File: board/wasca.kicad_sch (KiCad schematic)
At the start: 64 parts, among them CN1 CARTRIDGE_EDGE_CONNECTOR, CN2 TFP09-2-12B, CN3 Conn_02x02_Odd_Even, CN4 SODIMM-200, CN5 693063020911, U1 74ALVC164245, U10 SN74LVC1T45DBV, U11 SN74LVC1T45DBV, U12 SN74LVC1T45DBV, U13 ESP32_CAM_HALF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

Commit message: "Endorsed  by SHIRO!" logo
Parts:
- added SHIRO!1: SHIRO_LOGO, wasca:SHIRO!, symbol wasca:KICAD_LOGO
- TP2: value (none) -> TestPoint; footprint (none) -> wasca:TEST_PAD
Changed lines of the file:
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@@
     (pin "B9")
+  )
+  (symbol (lib_id "wasca:KICAD_LOGO") (at 468.63 165.1 0) (unit 1)
+    (in_bom yes) (on_board yes)
+    (property "Reference" "SHIRO!1" (id 0) (at 476.9612 163.9316 0)
+      (effects (font (size 1.27 1.27)) (justify left))
+    )
+    (property "Value" "SHIRO_LOGO" (id 1) (at 476.9612 166.243 0)
+      (effects (font (size 1.27 1.27)) (justify left))
+    )
+    (property "Footprint" "wasca:SHIRO!" (id 2) (at 468.63 165.1 0))
+    (property "Datasheet" "" (id 3) (at 468.63 165.1 0)
+      (effects (font (size 1.27 1.27)) hide)
+    )
   )
   (symbol (lib_id "Device:R") (at 739.14 78.74 0) (mirror y) (unit 1)
@@
       (effects (font (size 1.27 1.27)) (justify left))
     )
-    (property "Value" "" (id 1) (at 716.28 192.2779 0)
-      (effects (font (size 1.27 1.27)) (justify left))
-    )
-    (property "Footprint" "" (id 2) (at 718.82 194.31 0)
+    (property "Value" "TestPoint" (id 1) (at 716.28 192.2779 0)
+      (effects (font (size 1.27 1.27)) (justify left))
+    )
+    (property "Footprint" "wasca:TEST_PAD" (id 2) (at 718.82 194.31 0)
       (effects (font (size 1.27 1.27)) hide)
     )
@@
       (reference "SEGATA1") (unit 1) (value "LOGO") (footprint "wasca:Segata_Sanshiro")
     )
+    (path "/4f18e9dd-59f1-4eb2-8a59-104ed488d908"
+      (reference "SHIRO!1") (unit 1) (value "SHIRO_LOGO") (footprint "wasca:SHIRO!")
+    )
     (path "/d276ace0-aa98-4013-94e5-a87cfcb3830a"

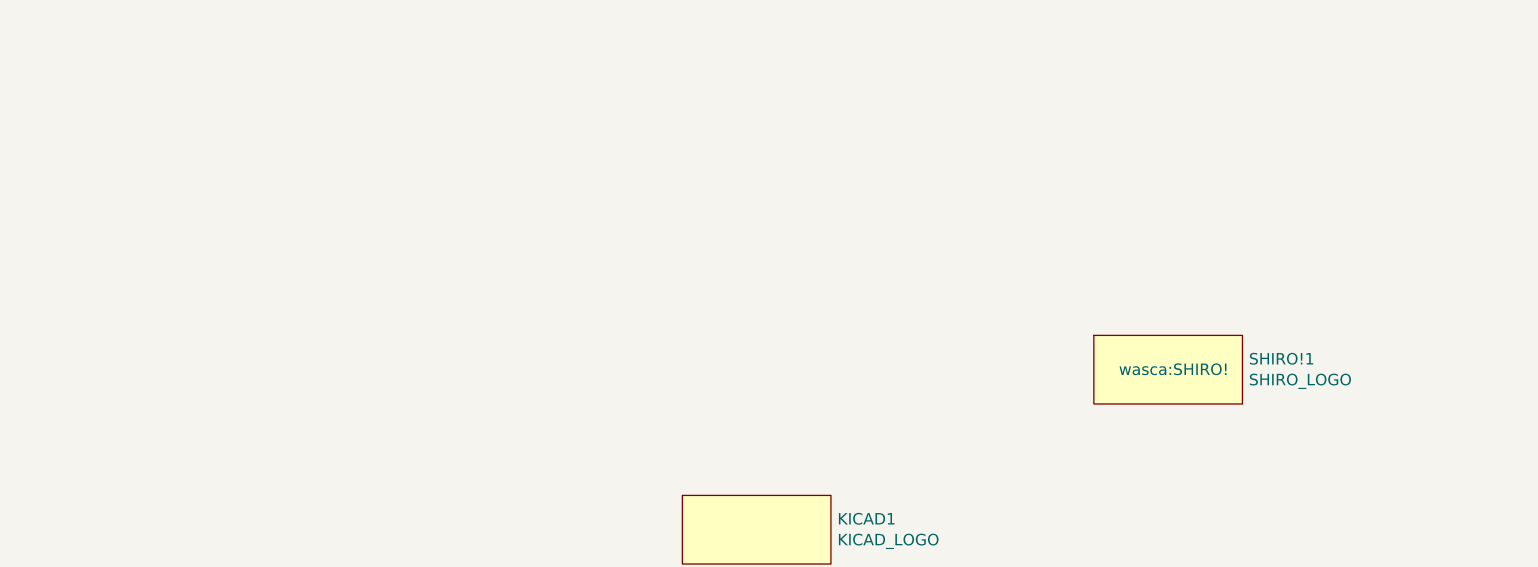
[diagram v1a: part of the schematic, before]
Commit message: Logo update
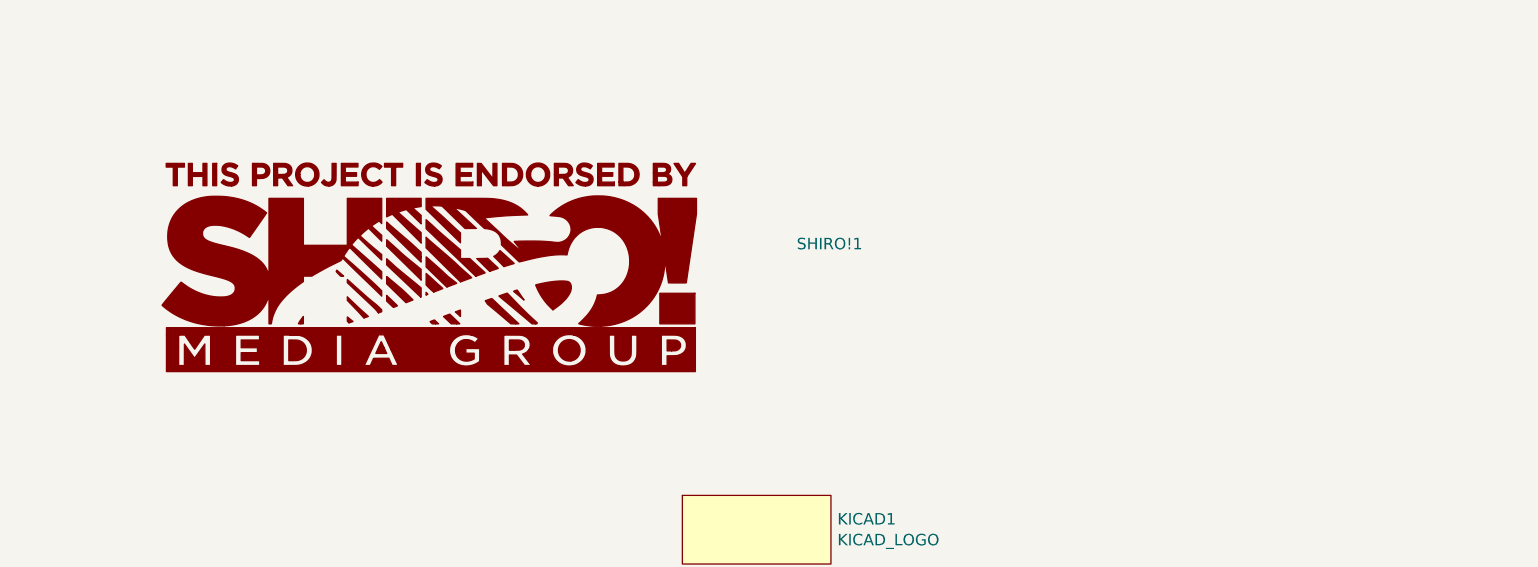
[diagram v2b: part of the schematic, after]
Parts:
- SHIRO!1: value SHIRO_LOGO -> (none); footprint wasca:SHIRO! -> (none); symbol wasca:KICAD_LOGO -> shiro!:LOGO
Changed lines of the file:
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@@
     (pin "B9")
   )
-  (symbol (lib_id "wasca:KICAD_LOGO") (at 468.63 165.1 0) (unit 1)
+  (symbol (lib_id "shiro!:LOGO") (at 386.08 153.67 0) (unit 1)
     (in_bom yes) (on_board yes)
-    (property "Reference" "SHIRO!1" (id 0) (at 476.9612 163.9316 0)
+    (property "Reference" "SHIRO!1" (id 0) (at 426.72 151.13 0)
       (effects (font (size 1.27 1.27)) (justify left))
     )
-    (property "Value" "SHIRO_LOGO" (id 1) (at 476.9612 166.243 0)
+    (property "Value" "" (id 1) (at 422.91 156.21 0)
       (effects (font (size 1.27 1.27)) (justify left))
     )
-    (property "Footprint" "wasca:SHIRO!" (id 2) (at 468.63 165.1 0))
-    (property "Datasheet" "" (id 3) (at 468.63 165.1 0)
+    (property "Footprint" "" (id 2) (at 386.08 153.67 0)
       (effects (font (size 1.27 1.27)) hide)
     )
+    (property "Datasheet" "" (id 3) (at 386.08 153.67 0)
+      (effects (font (size 1.27 1.27)) hide)
+    )

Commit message: Migrating to Kicad 7
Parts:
- SHIRO!1: value (none) -> SHIRO_LOGO; footprint (none) -> wasca:SHIRO!

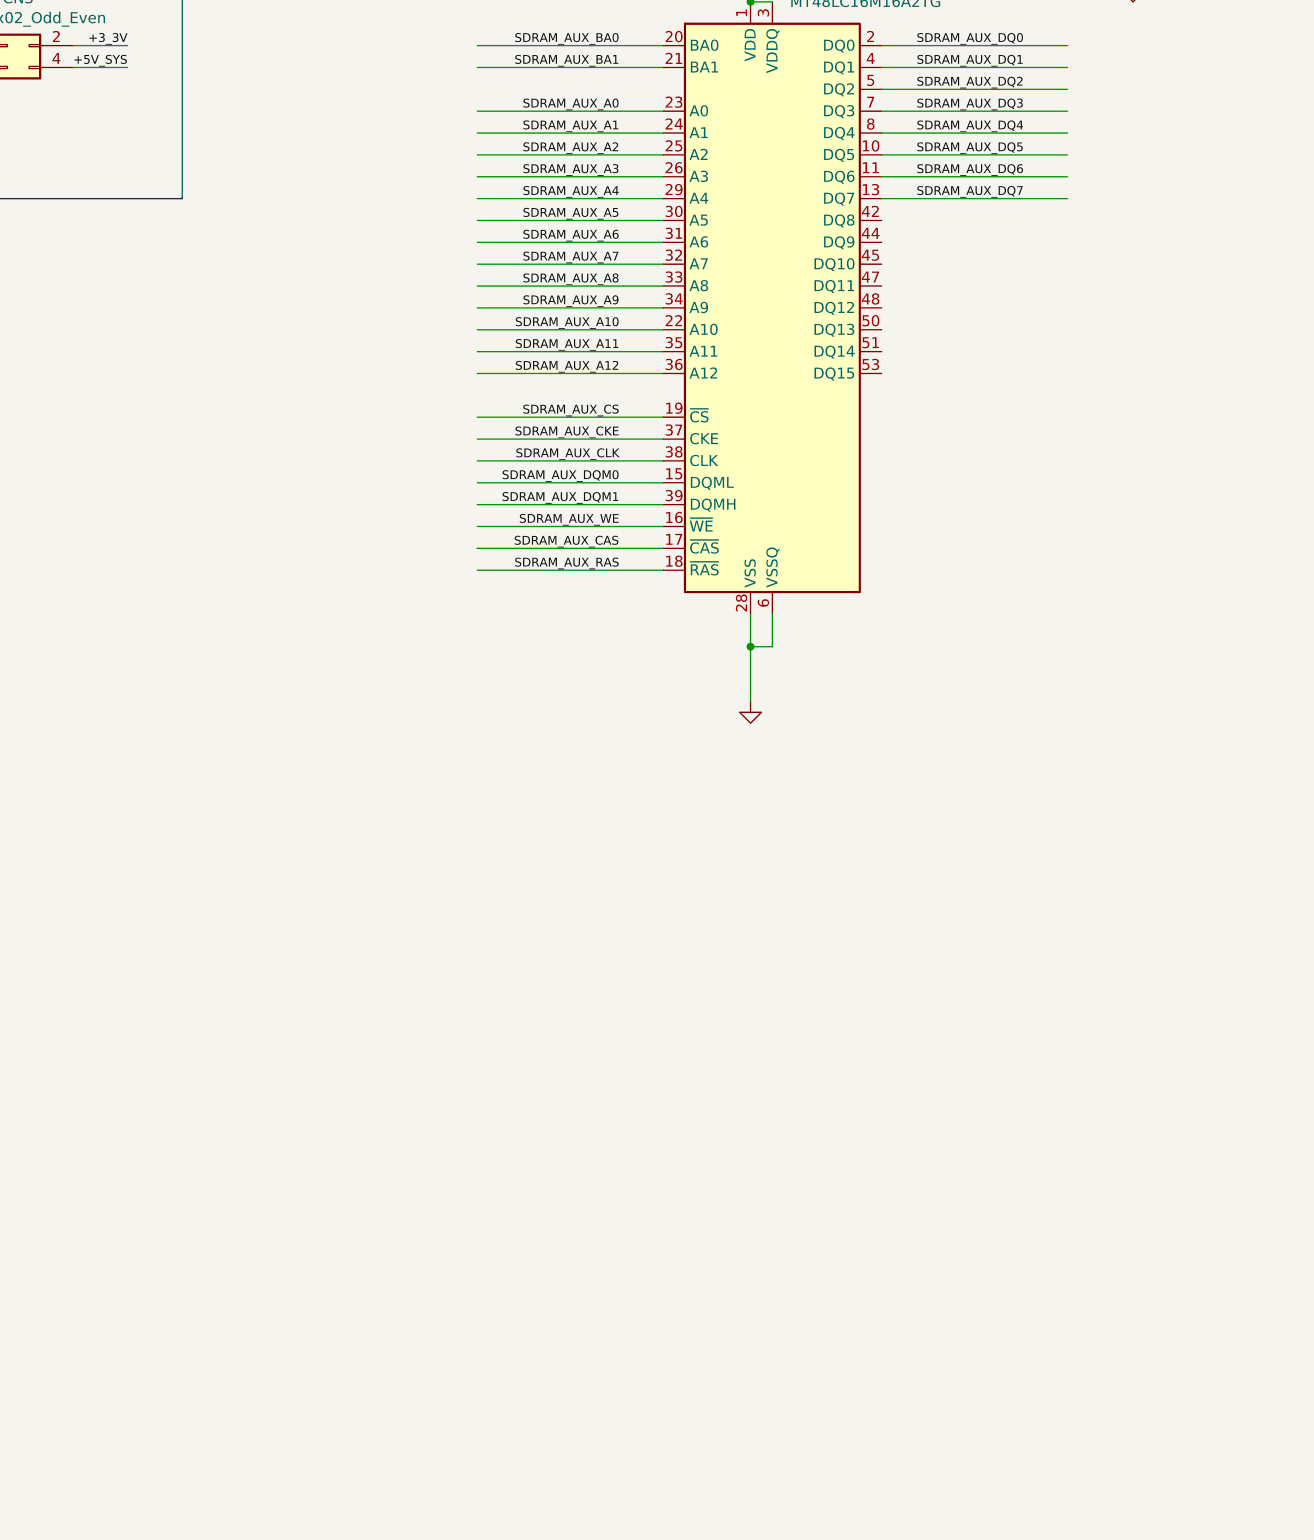
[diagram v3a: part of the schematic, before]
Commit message: Adding HyperRAM as an alternative for SDRAM
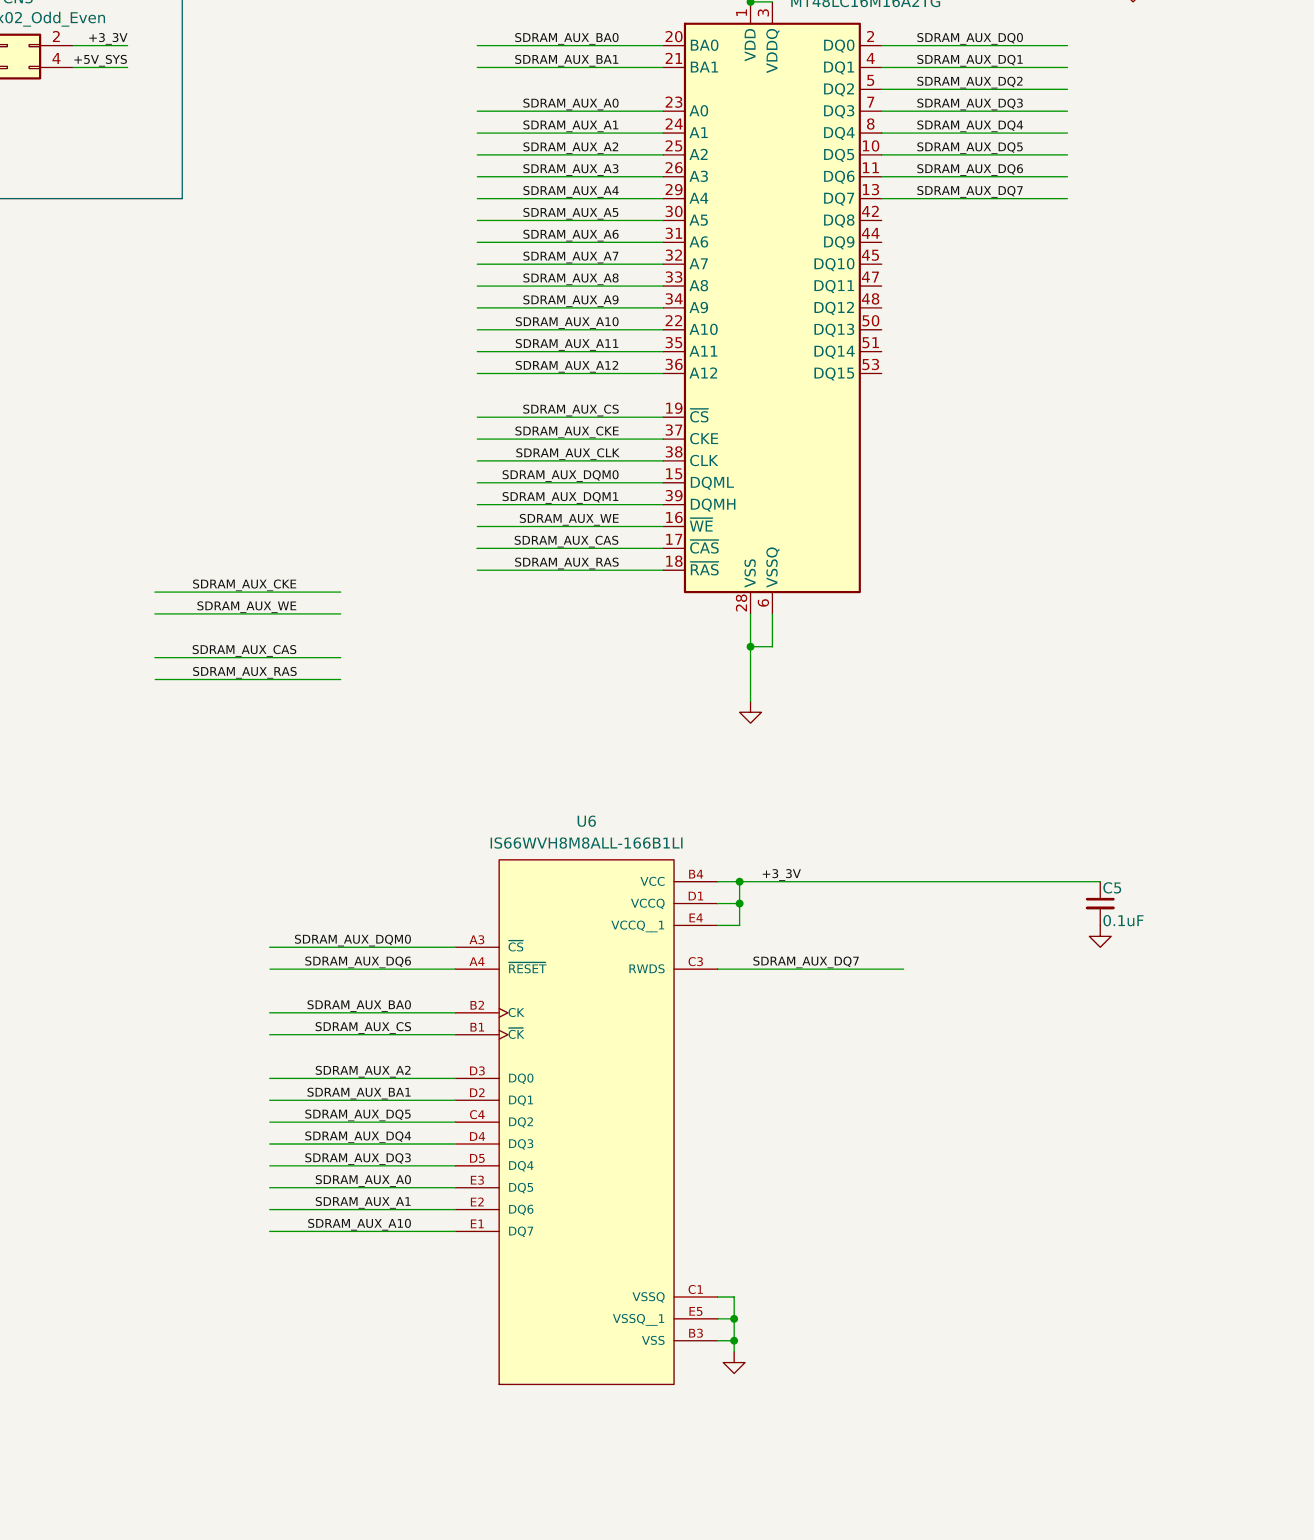
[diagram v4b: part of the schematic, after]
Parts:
- added C5: 0.1uF, Capacitor_SMD:C_0603_1608Metric_Pad1.08x0.95mm_HandSolder, symbol Device:C_Small
- added U6: IS66WVH8M8ALL-166B1LI, wasca:BGA25C100P5X5_800X600X120N, symbol IS66WVH8M8ALL-166B1LI:IS66WVH8M8ALL-166B1LI
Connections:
- net +3_3V: now also C5.1, U6.B4 (VCC), U6.D1 (VCCQ), U6.E4 (VCCQ__1)
- net GND: now also C5.2, U6.B3 (VSS), U6.C1 (VSSQ), U6.E5 (VSSQ__1)
- net SDRAM_AUX_A0: now also U6.E3 (DQ5)
- net SDRAM_AUX_A1: now also U6.E2 (DQ6)
- net SDRAM_AUX_A10: now also U6.E1 (DQ7)
- net SDRAM_AUX_A2: now also U6.D3 (DQ0)
- net SDRAM_AUX_BA0: now also U6.B2 (CK)
- net SDRAM_AUX_BA1: now also U6.D2 (DQ1)
- net SDRAM_AUX_CS: now also U6.B1 (~{CK})
- net SDRAM_AUX_DQ3: now also U6.D5 (DQ4)
- net SDRAM_AUX_DQ4: now also U6.D4 (DQ3)
- net SDRAM_AUX_DQ5: now also U6.C4 (DQ2)
- net SDRAM_AUX_DQ6: now also U6.A4 (~{RESET})
- net SDRAM_AUX_DQ7: now also U6.C3 (RWDS)
- net SDRAM_AUX_DQM0: now also U6.A3 (~{CS})

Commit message: Further cleanup
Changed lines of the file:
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@@
     (stroke (width 0) (type default))
   )
-  (wire (pts (xy 372.745 374.65) (xy 351.155 374.65))
-    (stroke (width 0) (type default))
-  )
   (wire (pts (xy 233.68 140.97) (xy 236.22 140.97))
     (stroke (width 0) (type default))
@@
     (stroke (width 0) (type default))
   )
-  (wire (pts (xy 372.745 372.11) (xy 351.155 372.11))
-    (stroke (width 0) (type default))
-  )
   (wire (pts (xy 736.6 349.25) (xy 768.35 349.25))
     (stroke (width 0) (type default))
@@
     (stroke (width 0) (type default))
   )
-  (wire (pts (xy 372.745 382.27) (xy 351.1989 382.27))
-    (stroke (width 0) (type default))
-  )
   (wire (pts (xy 135.89 82.55) (xy 138.43 82.55))
     (stroke (width 0) (type default))
@@
     (stroke (width 0) (type default))
   )
-  (wire (pts (xy 372.745 379.73) (xy 351.155 379.73))
-    (stroke (width 0) (type default))
-  )
   (wire (pts (xy 82.55 215.9) (xy 101.6 215.9))
     (stroke (width 0) (type default))
@@
     (effects (font (size 1.016 1.016)) (justify right bottom))
   )
-  (label "SDRAM_AUX_CKE" (at 367.665 372.11 180) (fields_autoplaced)
-    (effects (font (size 1.016 1.016)) (justify right bottom))
-  )
   (label "ABUS_D13" (at 143.51 226.06 0) (fields_autoplaced)
     (effects (font (size 1.016 1.016)) (justify left bottom))
@@
     (effects (font (size 1.016 1.016)) (justify right bottom))
   )
-  (label "SDRAM_AUX_CAS" (at 367.665 379.73 180) (fields_autoplaced)
-    (effects (font (size 1.016 1.016)) (justify right bottom))
-  )
   (label "SDRAM_AUX_CAS" (at 405.0861 367.03 180) (fields_autoplaced)
     (effects (font (size 1.016 1.016)) (justify right bottom))
   )
-  (label "SDRAM_AUX_WE" (at 367.665 374.65 180) (fields_autoplaced)
-    (effects (font (size 1.016 1.016)) (justify right bottom))
-  )
-  (label "SDRAM_AUX_RAS" (at 367.7089 382.27 180) (fields_autoplaced)
-    (effects (font (size 1.016 1.016)) (justify right bottom))
-  )

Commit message: Further cleanup
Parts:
- removed TP1, TP2: TestPoint, wasca:TEST_PAD, symbol Connector:TestPoint
- added CN6: Conn_01x02_Pin, Connector_PinHeader_2.54mm:PinHeader_1x02_P2.54mm_Vertical, symbol Connector:Conn_01x02_Pin
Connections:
- net TEST_2: now reaches CN4.150
- net TEST_2: now also CN6.2 (Pin_2)
- net TEST_1: now reaches CN4.89
- net TEST_1: now also CN6.1 (Pin_1)

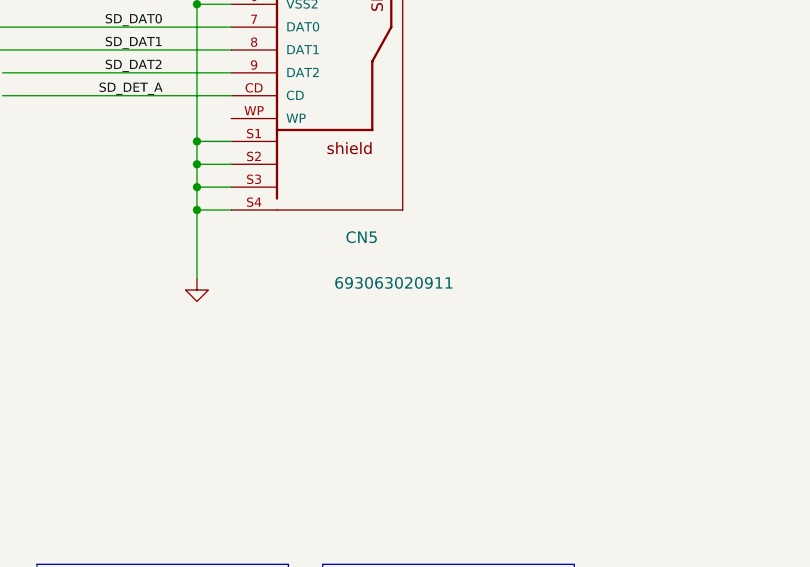
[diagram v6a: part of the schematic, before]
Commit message: Migrating to Kicad 10
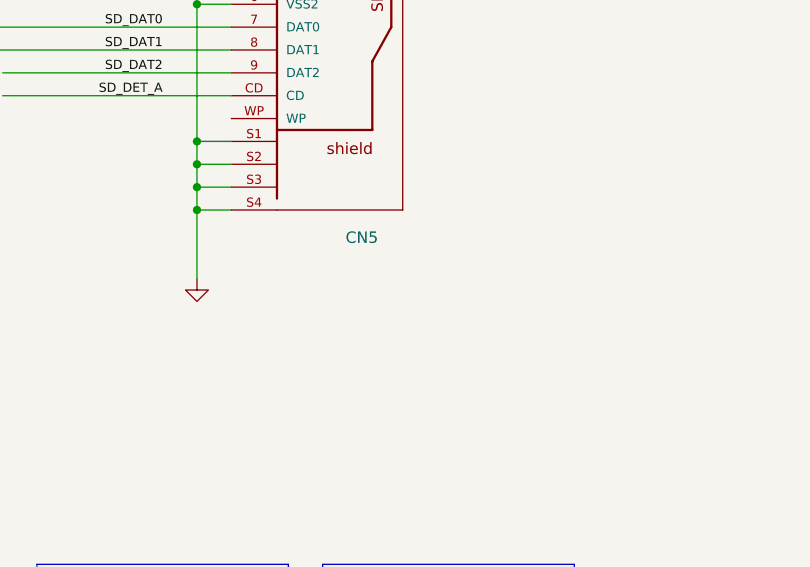
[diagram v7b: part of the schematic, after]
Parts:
- CN5: VALUE 693063020911 -> (none)
